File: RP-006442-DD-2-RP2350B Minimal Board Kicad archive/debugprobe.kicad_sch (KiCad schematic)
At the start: 41 parts, among them J5 USB_C_Receptacle_USB2.0_16P, J6 Conn_02x18_Odd_Even, J7 SM03B-SRSS-TB, J8 Conn_02x18_Odd_Even, SW3 SW_Push, SW4 SW_Push, U5 W25Q128JVS, U6 NCP1117-3.3_SOT223, U7 RP2350_60QFN, Y2 ABM8-272-T3

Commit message: added leds schematic page
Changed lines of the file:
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@@
 (kicad_sch
-	(version 20231120)
+	(version 20250114)
 	(generator "eeschema")
-	(generator_version "8.0")
+	(generator_version "9.0")
 	(paper "A3")
+	(circle
+		(center 140.335 110.49)
+		(radius 0.635)
+		(stroke
+			(width 0)
+			(type default)
+			(color 132 0 0 1)
+		)
+		(fill
+			(type color)
+			(color 132 0 0 1)
+		)
+	)
+	(text "Power"
+		(exclude_from_sim no)
+		(at 78.74 29.21 0)
+		(effects
+			(font
+				(size 2.54 2.54)
+			)
+			(justify left bottom)
+		)
+	)
+	(text "Flash"
+		(exclude_from_sim no)
+		(at 36.83 119.38 0)
+		(effects
+			(font
+				(size 2.54 2.54)
+			)
+			(justify left bottom)
+		)
+	)
+	(text "Make sure R7 and R8 are close to RP2350\n"
+		(exclude_from_sim no)
+		(at 259.715 104.775 0)
+		(effects
+			(font
+				(size 1.27 1.27)
+			)
+			(justify left bottom)
+		)
+	)
+	(text "12MHz Crystal"
+		(exclude_from_sim no)
+		(at 85.09 226.695 0)
+		(effects
+			(font
+				(size 2.54 2.54)
+			)
+			(justify left bottom)
+		)
+	)
+	(text "IOs"
+		(exclude_from_sim no)
+		(at 354.965 114.935 0)
+		(effects
+			(font
+				(size 2.54 2.54)
+			)
+			(justify left bottom)
+		)
+	)
+	(text "JST Debug Connector"
+		(exclude_from_sim no)
+		(at 328.295 196.215 0)
+		(effects
+			(font
+				(size 1.27 1.27)
+			)
+			(justify left bottom)
+		)
+	)
 	(junction
 		(at 211.455 85.725)
@@
 		)
 	)
-	(circle
-		(center 140.335 110.49)
-		(radius 0.635)
-		(stroke
-			(width 0)
-			(type default)
-			(color 132 0 0 1)
-		)
-		(fill
-			(type color)
-			(color 132 0 0 1)
-		)
-	)
-	(text "Power"
-		(exclude_from_sim no)
-		(at 78.74 29.21 0)
-		(effects
-			(font
-				(size 2.54 2.54)
-			)
-			(justify left bottom)
-		)
-	)
-	(text "Flash"
-		(exclude_from_sim no)
-		(at 36.83 119.38 0)
-		(effects
-			(font
-				(size 2.54 2.54)
-			)
-			(justify left bottom)
-		)
-	)
-	(text "Make sure R7 and R8 are close to RP2350\n"
-		(exclude_from_sim no)
-		(at 259.715 104.775 0)
-		(effects
-			(font
-				(size 1.27 1.27)
-			)
-			(justify left bottom)
-		)
-	)
-	(text "12MHz Crystal"
-		(exclude_from_sim no)
-		(at 85.09 226.695 0)
-		(effects
-			(font
-				(size 2.54 2.54)
-			)
-			(justify left bottom)
-		)
-	)
-	(text "IOs"
-		(exclude_from_sim no)
-		(at 354.965 114.935 0)
-		(effects
-			(font
-				(size 2.54 2.54)
-			)
-			(justify left bottom)
-		)
-	)
-	(text "JST Debug Connector"
-		(exclude_from_sim no)
-		(at 328.295 196.215 0)
-		(effects
-			(font
-				(size 1.27 1.27)
-			)
-			(justify left bottom)
-		)
-	)

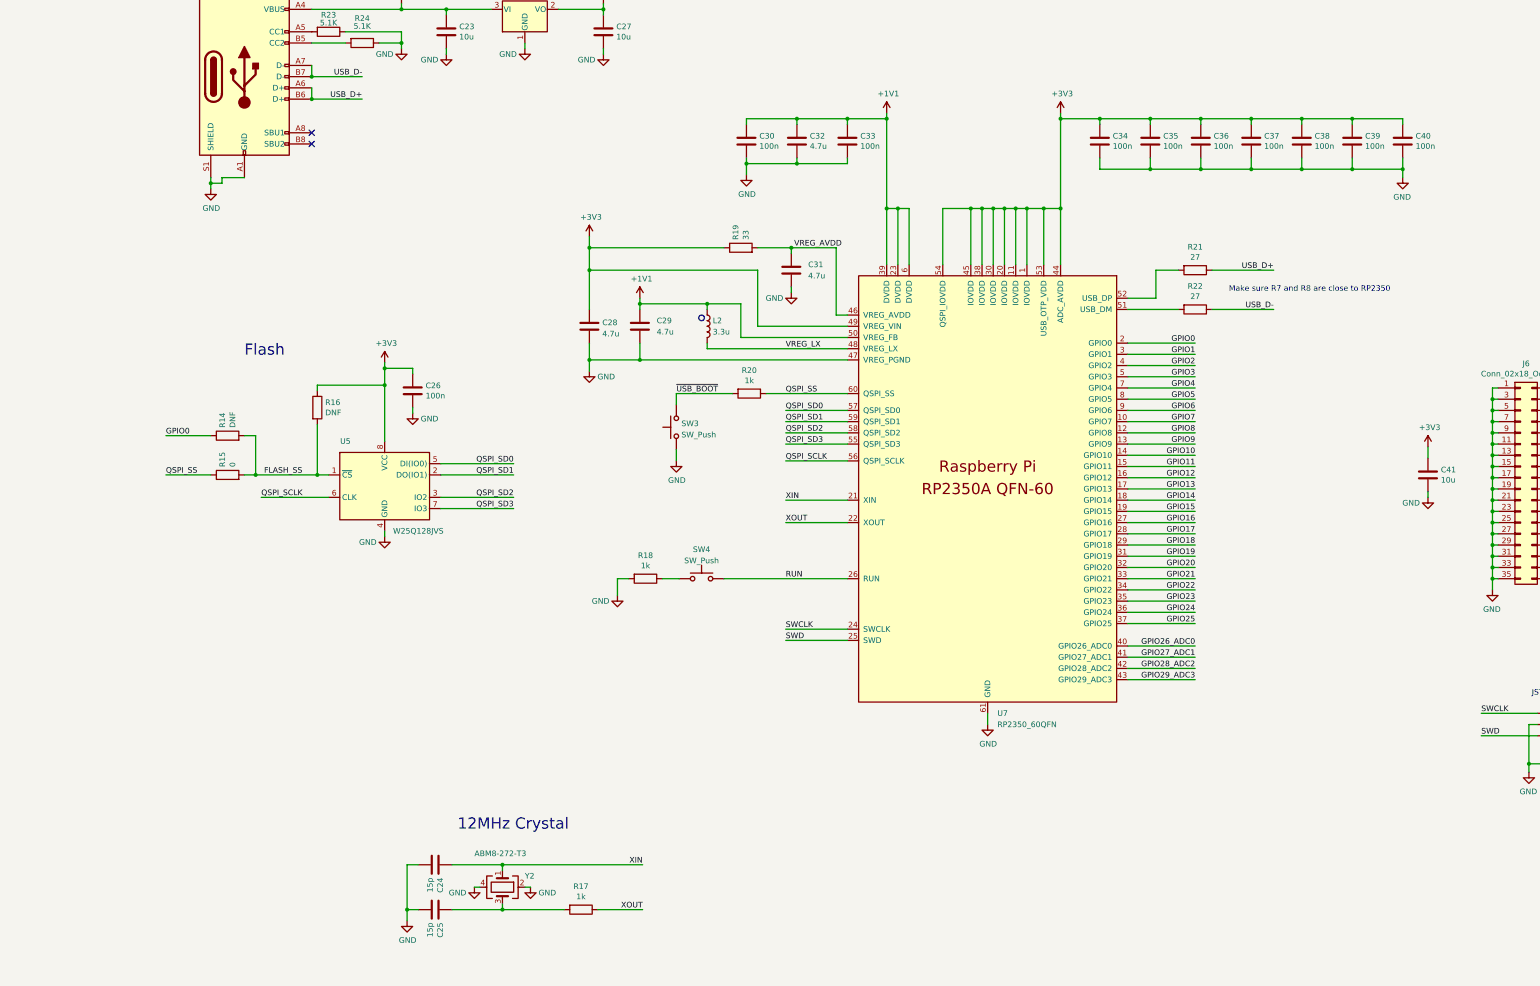
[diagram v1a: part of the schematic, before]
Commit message: Placed hierarchical labels in debugprobe
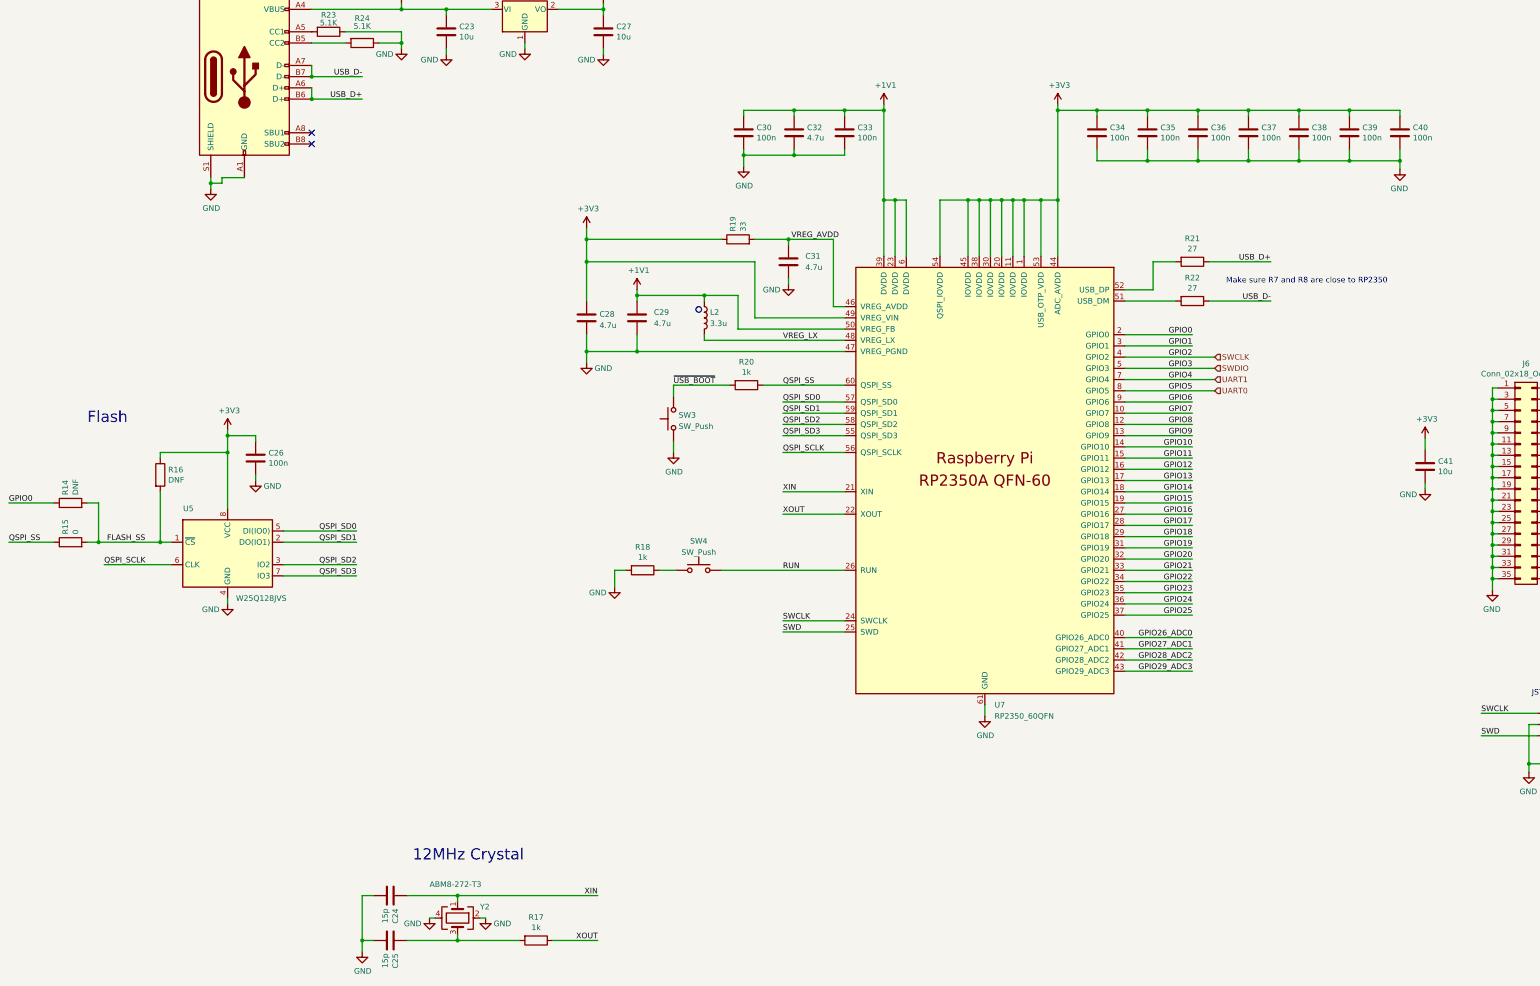
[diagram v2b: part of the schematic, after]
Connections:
- net GPIO2 is gone; now on net SWCLK: J6.8 (Pin_8), U7.4 (GPIO2)
- net GPIO3 renamed SWDIO
- net GPIO4 renamed UART1
- net GPIO5 renamed UART0
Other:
- moved on the sheet: C24, C25, C26, C28, C29, C30, C31, C32, C33, C34, C35, C36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

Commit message: Added debugger labels to root
moved some symbols around
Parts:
- removed J7: SM03B-SRSS-TB, Connector_JST:JST_SH_SM03B-SRSS-TB_1x03-1MP_P1.00mm_Horizontal, symbol Connector_Generic_MountingPin:Conn_01x03_MountingPin
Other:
- note removed: "JST Debug Connector"
- moved on the sheet: C26, J6, J8, R14, R15, R16, R18, SW4, U5

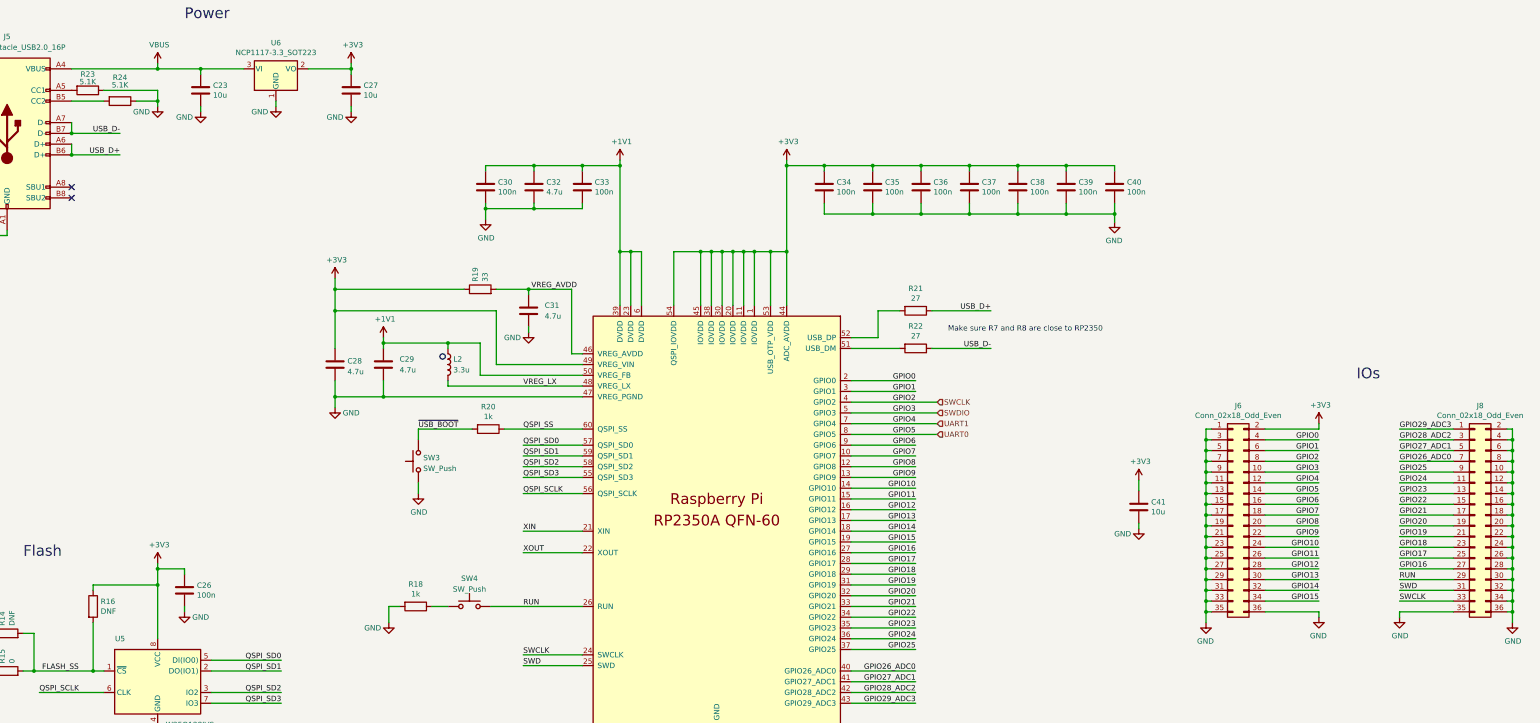
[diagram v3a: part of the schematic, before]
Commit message: Assigned footprints to symbols
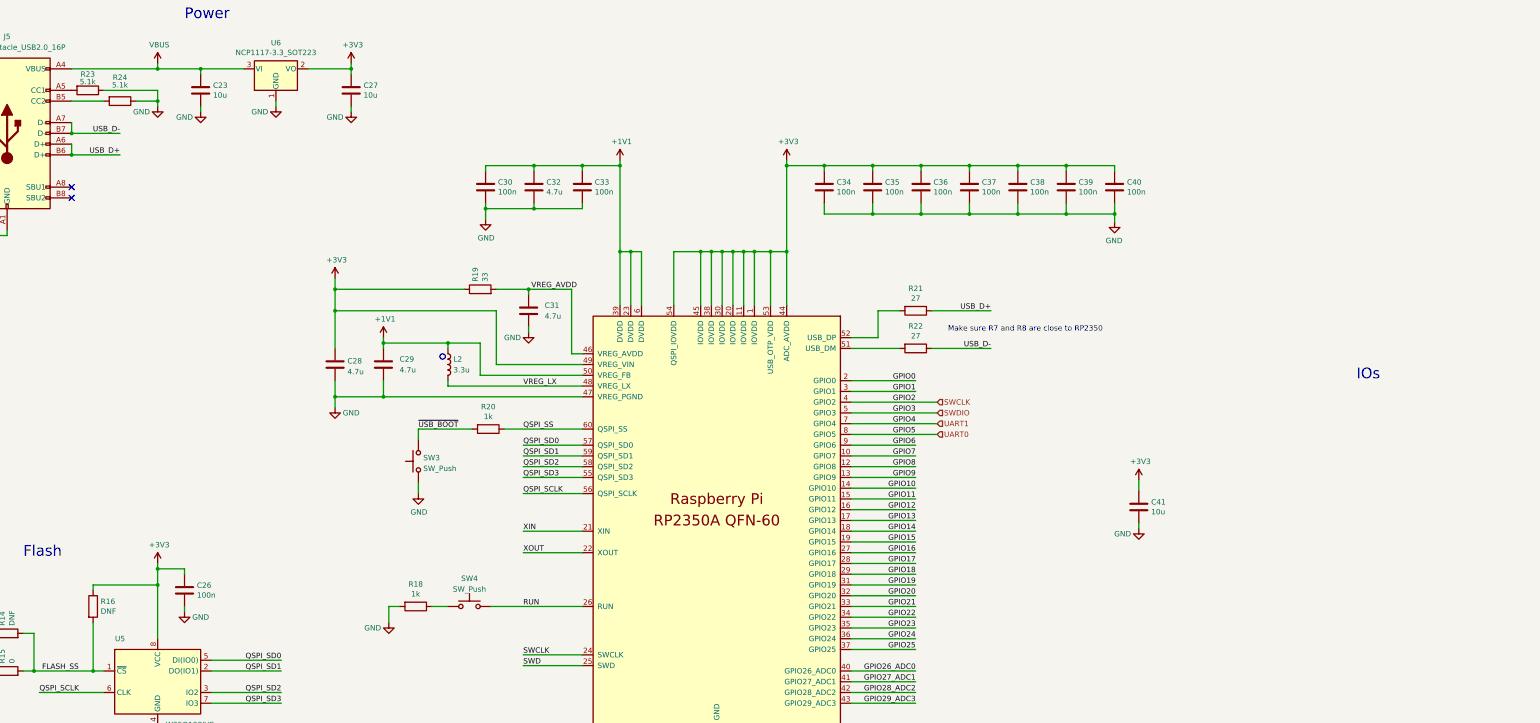
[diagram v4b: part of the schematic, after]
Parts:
- removed J6, J8: Conn_02x18_Odd_Even, Connector_PinHeader_2.54mm:PinHeader_2x18_P2.54mm_Vertical, symbol Connector_Generic:Conn_02x18_Odd_Even
- R23, R24: value 5.1K -> 5.1k; footprint (none) -> Resistor_SMD:R_0402_1005Metric

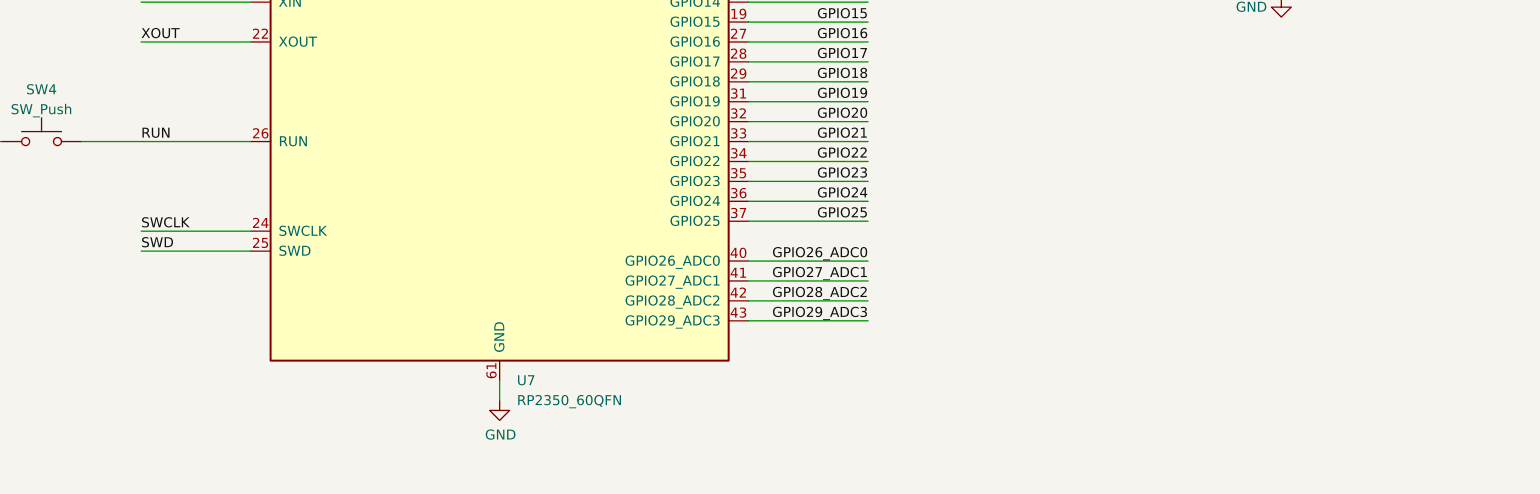
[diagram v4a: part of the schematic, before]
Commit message: Added debugprobe components to pcb
added pinheader connector to debug probe
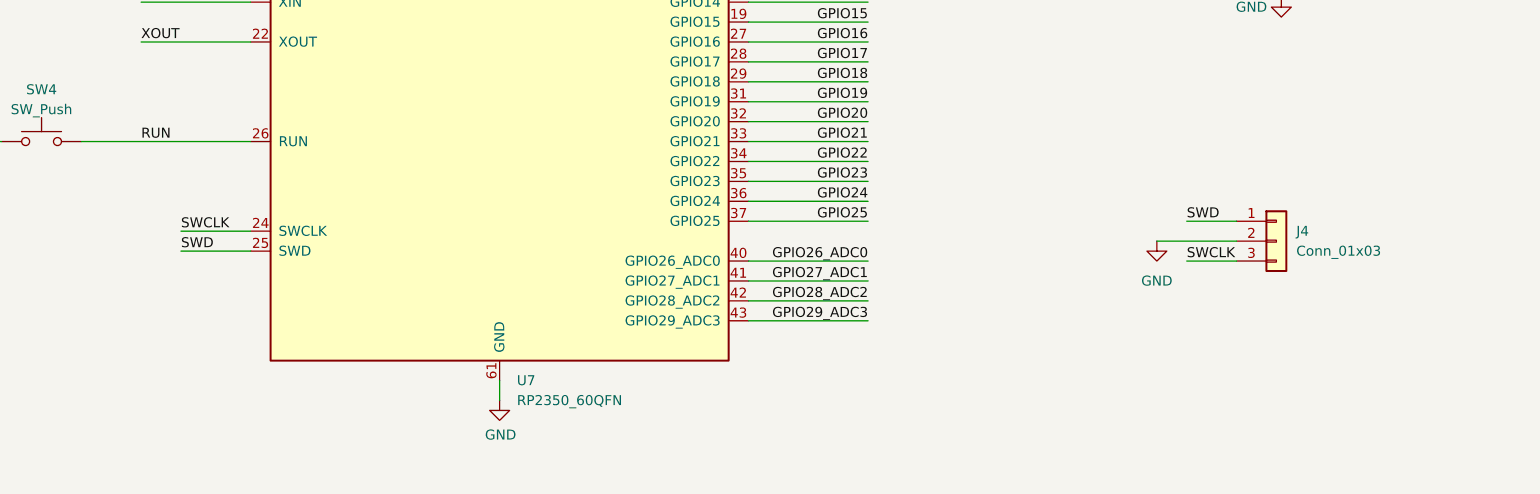
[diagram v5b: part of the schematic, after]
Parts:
- added J4: Conn_01x03, Connector_PinHeader_2.54mm:PinHeader_1x03_P2.54mm_Vertical, symbol Connector_Generic:Conn_01x03
- J5: footprint (none) -> Connector_USB:USB_C_Receptacle_HRO_TYPE-C-31-M-12
- U5: footprint Package_SO:SOIC-8_5.23x5.23mm_P1.27mm -> Package_SO:SOIC-8_5.3x5.3mm_P1.27mm
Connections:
- net GND: now also J4.2 (Pin_2)
- net SWCLK: now also J4.3 (Pin_3)
- net SWD: now also J4.1 (Pin_1)
